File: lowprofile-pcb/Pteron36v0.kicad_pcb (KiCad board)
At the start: 2 copper layers, 127.8 x 97.9 mm, 43 parts, among them J1 AudioJack4, J2 AudioJack4, SW10 SW_PUSH, SW12 SW_PUSH, SW13 SW_PUSH, SW14 SW_PUSH, SW15 SW_PUSH, SW17 SW_PUSH, SW18 SW_PUSH, SW19 SW_PUSH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

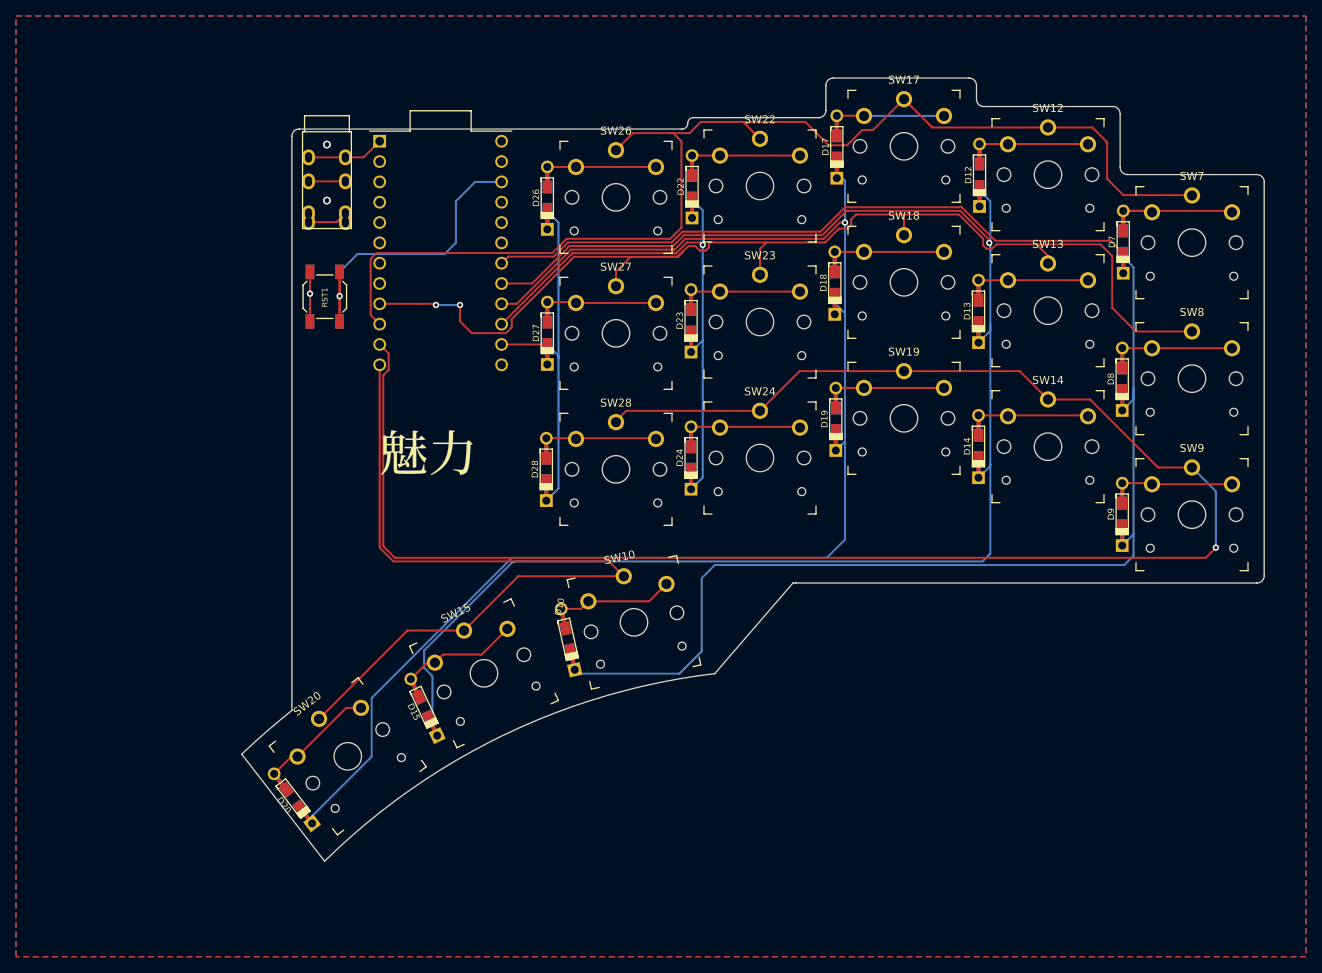
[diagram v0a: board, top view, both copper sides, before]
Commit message: cleaner tracing
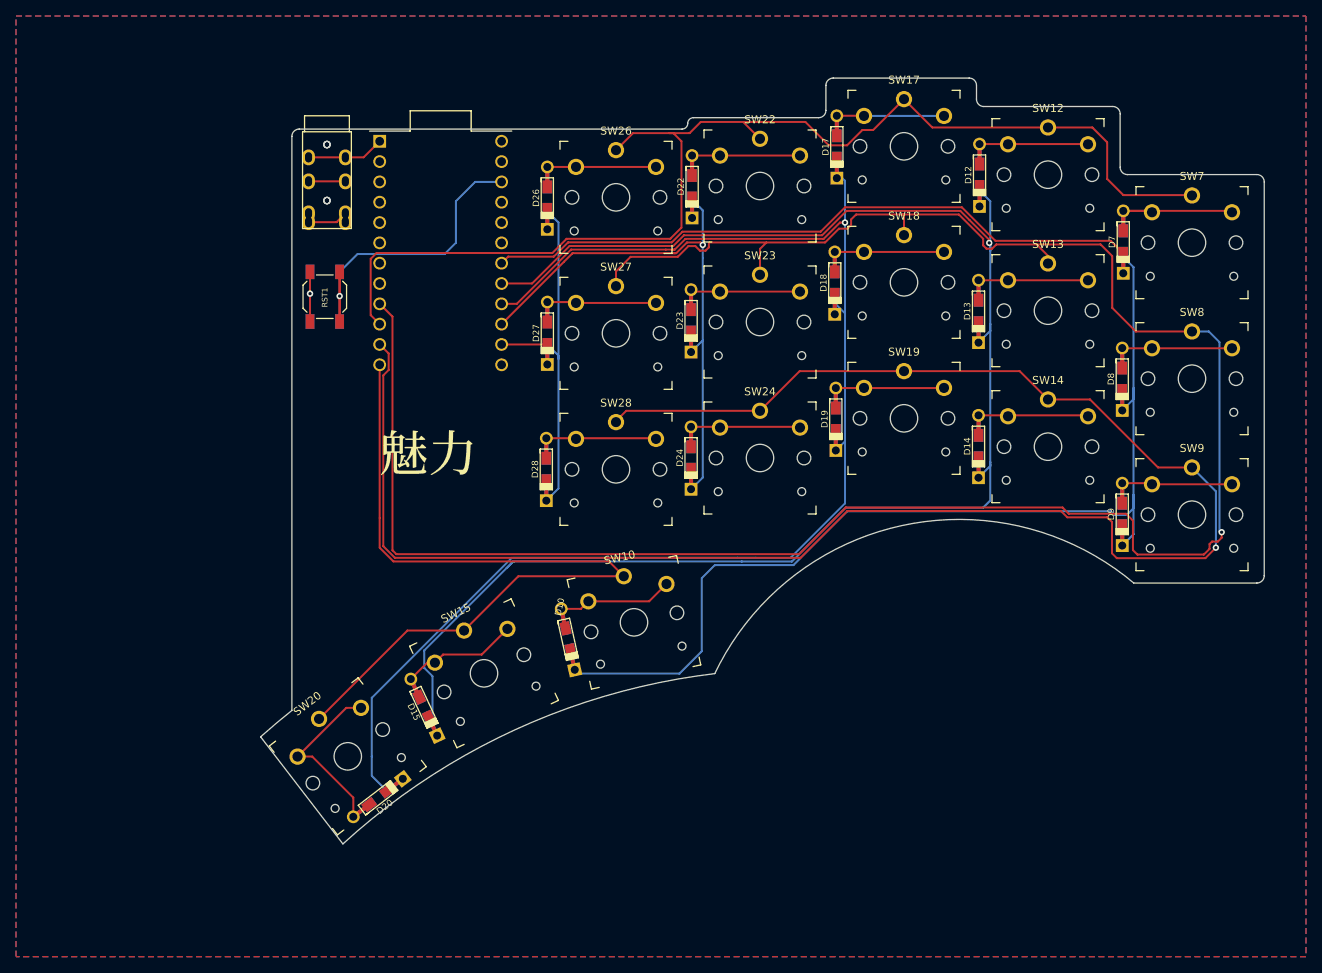
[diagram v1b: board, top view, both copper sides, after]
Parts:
- moved D20 10.6 mm to (132.3, 131.7), turned to 37.5 degrees
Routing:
- net /Row2: track 144.2 -> 270.9 mm, vias 2 -> 1
- net /Col3: track 183.2 -> 174.1 mm
- net Net-(D20-Pad2): track 14.3 -> 22.7 mm
- net /Row3: track 222.1 -> 229.3 mm
- net /Col2: track 204.1 -> 201.8 mm
- net /Col1: track 207.5 -> 209.3 mm
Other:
- board size 127.8 x 97.9 mm -> 125.5 x 95.7 mm
- net class Default removed

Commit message: updated board outline and wiring
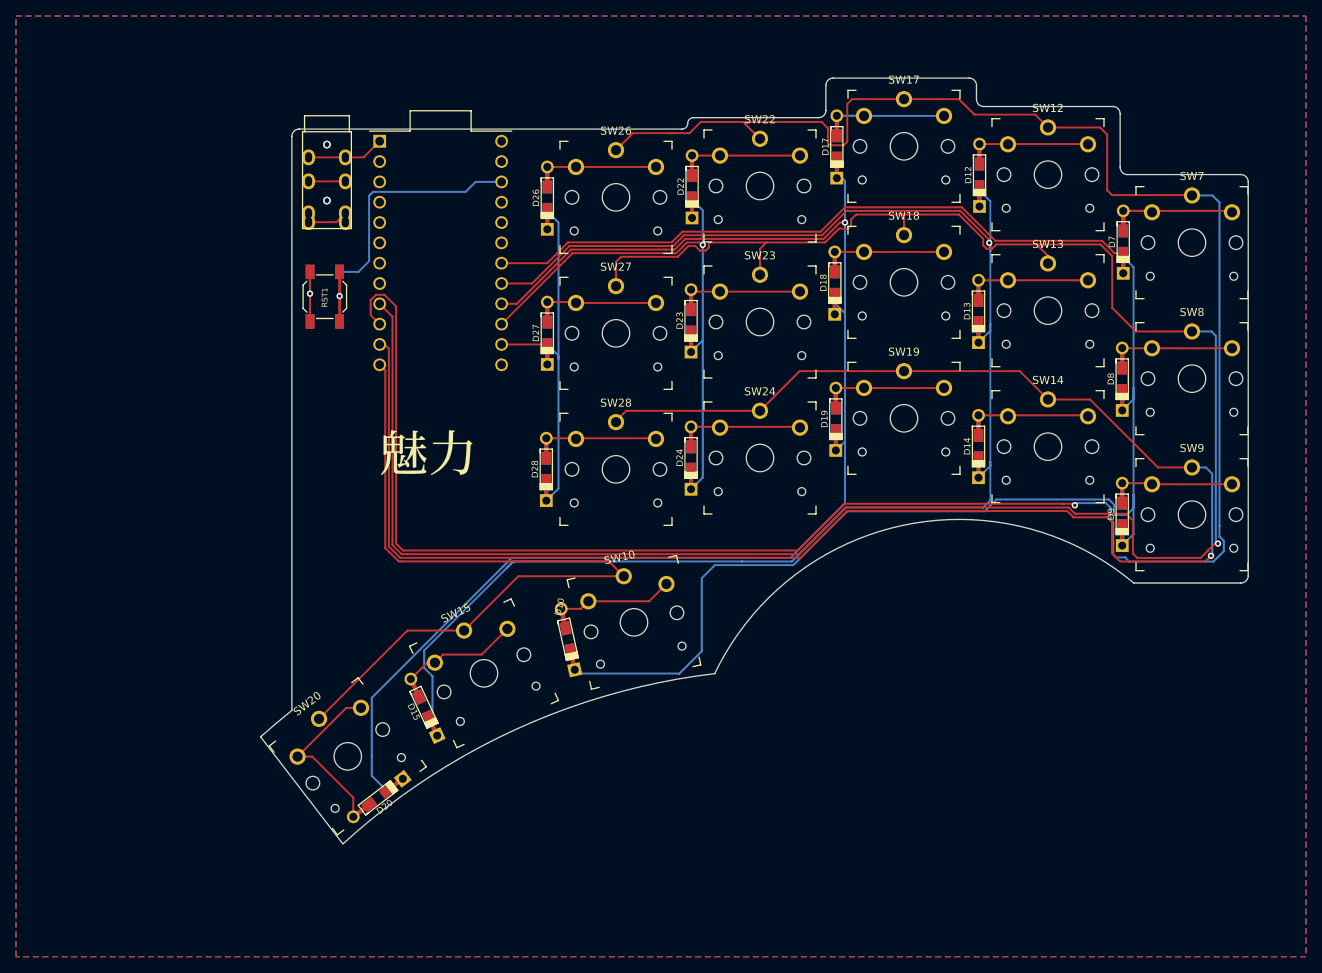
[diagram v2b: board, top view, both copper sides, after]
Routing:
- net /Row1: track 149.5 -> 291.7 mm, vias 0 -> 1
- net /Col1: track 209.3 -> 211.2 mm
- net Net-(RST1-Pad1): track 46.6 -> 48.3 mm
- net /Row3: track 229.3 -> 229.9 mm
- net /Row2: track 270.9 -> 271.5 mm
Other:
- board size 125.5 x 95.7 mm -> 123.5 x 95.7 mm

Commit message: update outline with curves, cleaup wiring
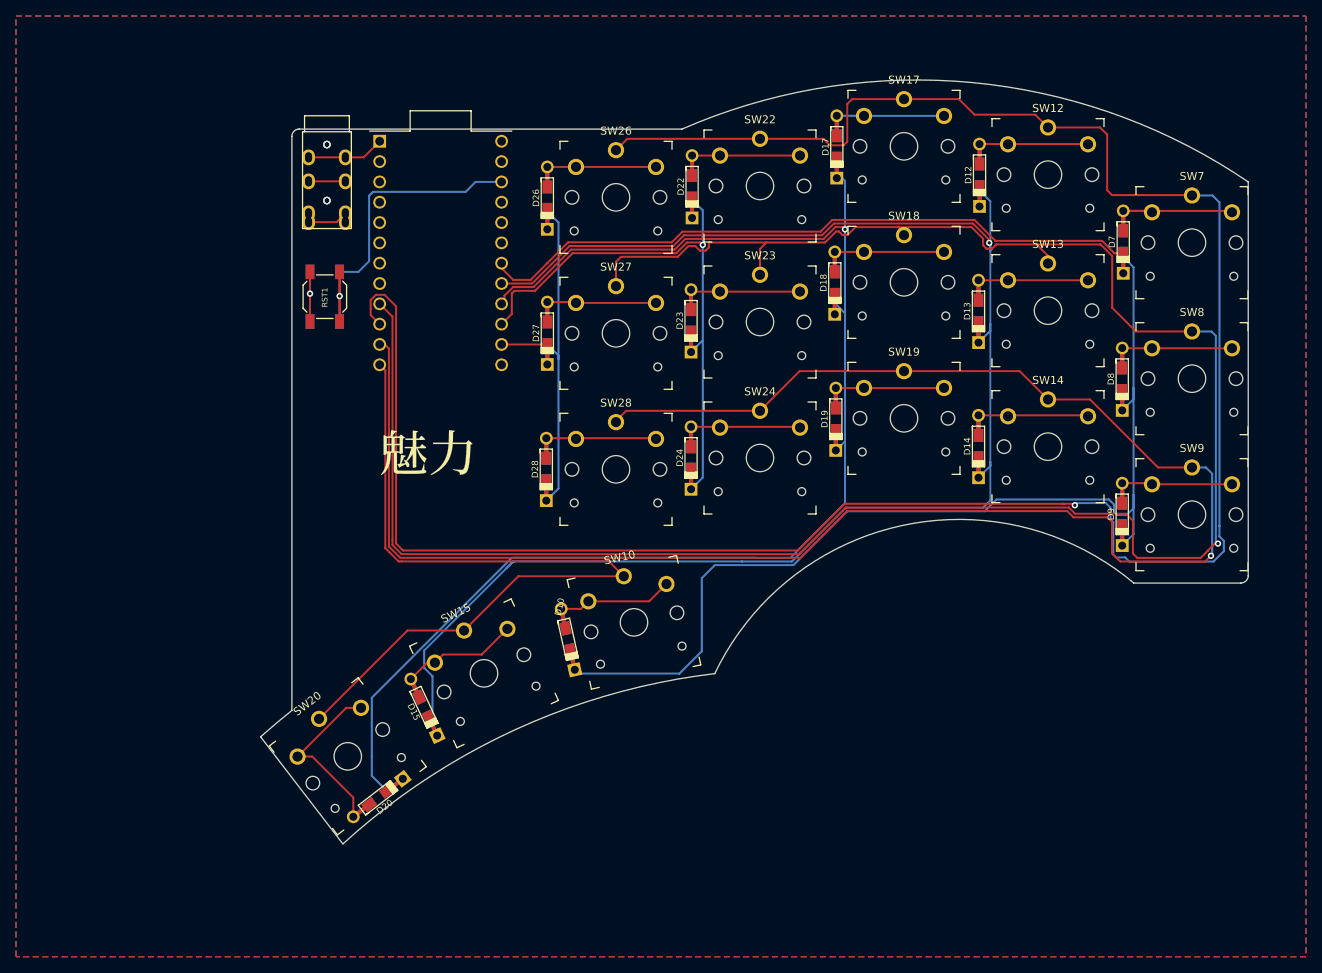
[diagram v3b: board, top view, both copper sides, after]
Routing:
- net /Row1: track 291.7 -> 285.4 mm
- net /Row2: track 271.5 -> 268.8 mm
- net /Col4: track 70.0 -> 71.5 mm
- net /Col2: track 201.8 -> 200.5 mm
- net /Col1: track 211.2 -> 211.9 mm
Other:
- board size 123.5 x 95.7 mm -> 123.5 x 95.5 mm

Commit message: finalise art and board
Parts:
- added EN_1: Rotary_Encoder, Rotary_Encoder:RotaryEncoder_Alps_EC12E_Vertical_H20mm, F.Cu at (130.3, 87.6)
- added LOGO3: LOGO-OTL, personal-logo:peacock-medium, F.Cu at (139.3, 73.4)
- added LOGO4: LOGO-OTL, personal-logo:peacock-medium, B.Cu at (145.2, 85.0)
- moved LOGO1 14.8 mm to (145.2, 101.7)
- moved LOGO2 13.4 mm to (134.9, 102.1)
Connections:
- U1 pad 19: (no net) -> /RotB
- U1 pad 20: (no net) -> /RotA
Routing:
- net /RotB: track 0.00 -> 47.8 mm
- net /RotA: track 0.00 -> 46.1 mm
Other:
- board size 123.5 x 95.5 mm -> 123.5 x 95.6 mm

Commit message: add stl for 38 key variant case, add 1.5 u on lowprofile keyboard
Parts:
- removed LOGO1, LOGO2: LOGO-OTL, personal-logo:miryoku-kicad-small
- added SW1: SW_PUSH, keyswitches:PG1350_reversible, F.Cu at (126.8, 124.5)
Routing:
- net /Row4: track 99.9 -> 114.6 mm
- net Net-(D20-Pad2): track 22.7 -> 27.7 mm
